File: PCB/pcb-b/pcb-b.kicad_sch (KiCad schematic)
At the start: 25 parts, among them J1 Conn_02x05_Counter_Clockwise, J2 Conn_02x05_Counter_Clockwise, K1 HK19F-DCxxV-SHC, Q13 TPCA8120,L1Q, Q3 BC817, Q9 BC817

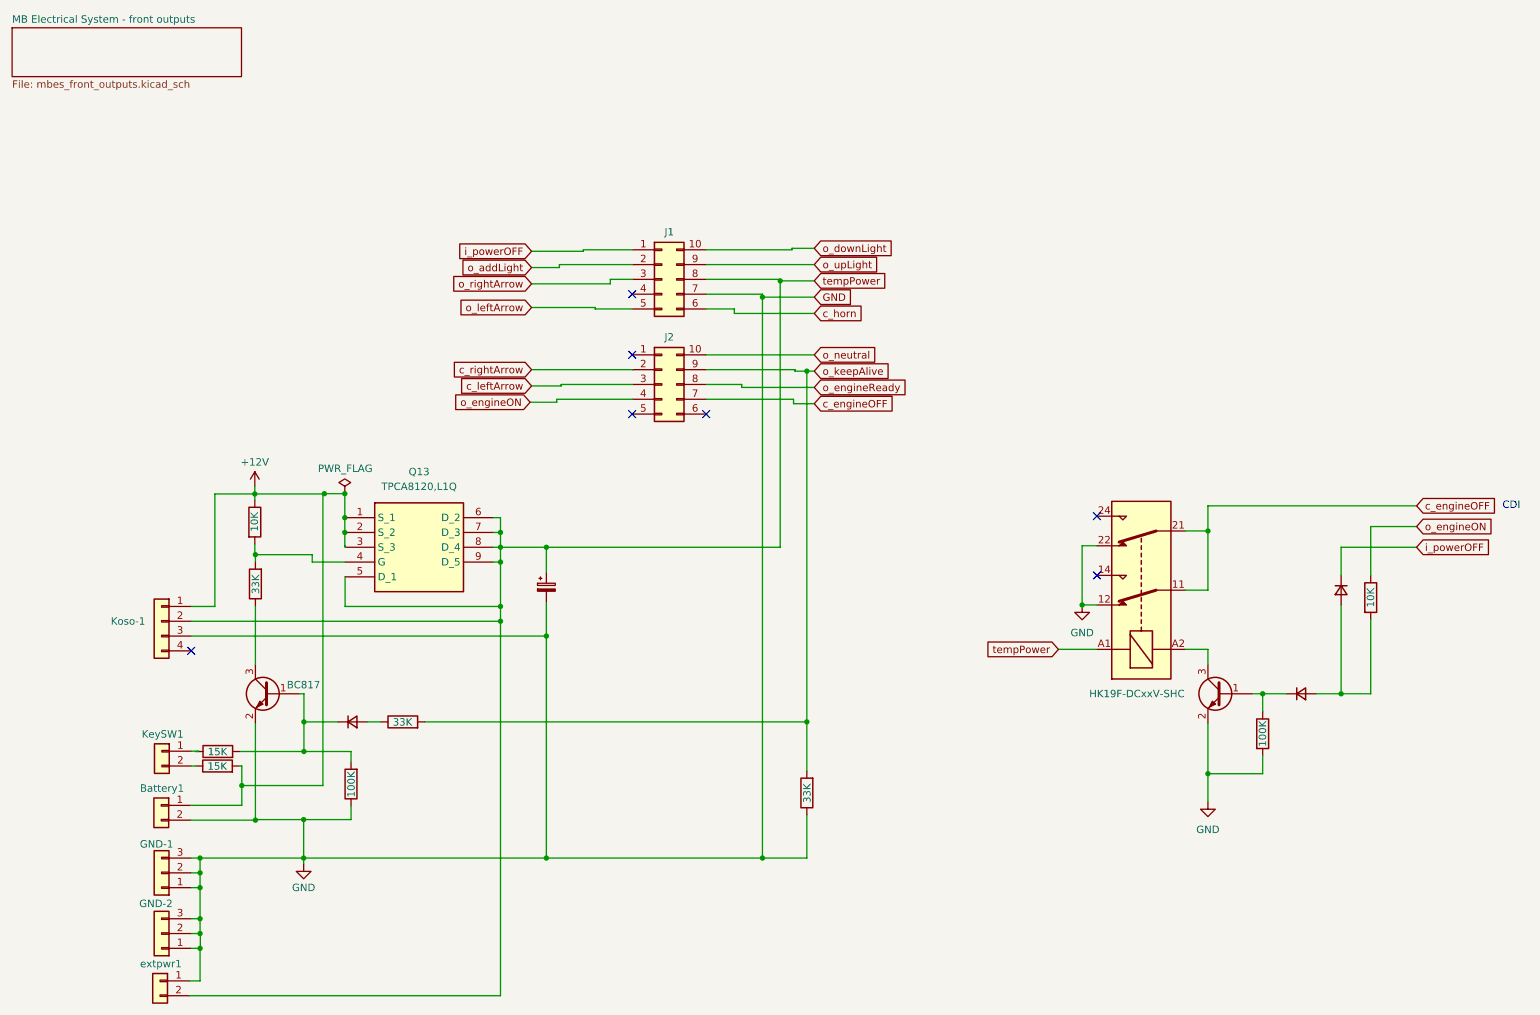
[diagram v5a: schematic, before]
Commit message: Many changes and fixes
Electric schema A & B
	- Wrong (undefined) signals direction fixed
	- More readable schema getting: c_<signal> color has changed
	- Some pull-up resistors has been added for safing purpose
	- Wire connectors holes size reducing
	- Because Led indicatord uses less then 500mA, their wire connectors have been substituted by pin-header ones

PCB
	- Updates for schema changes
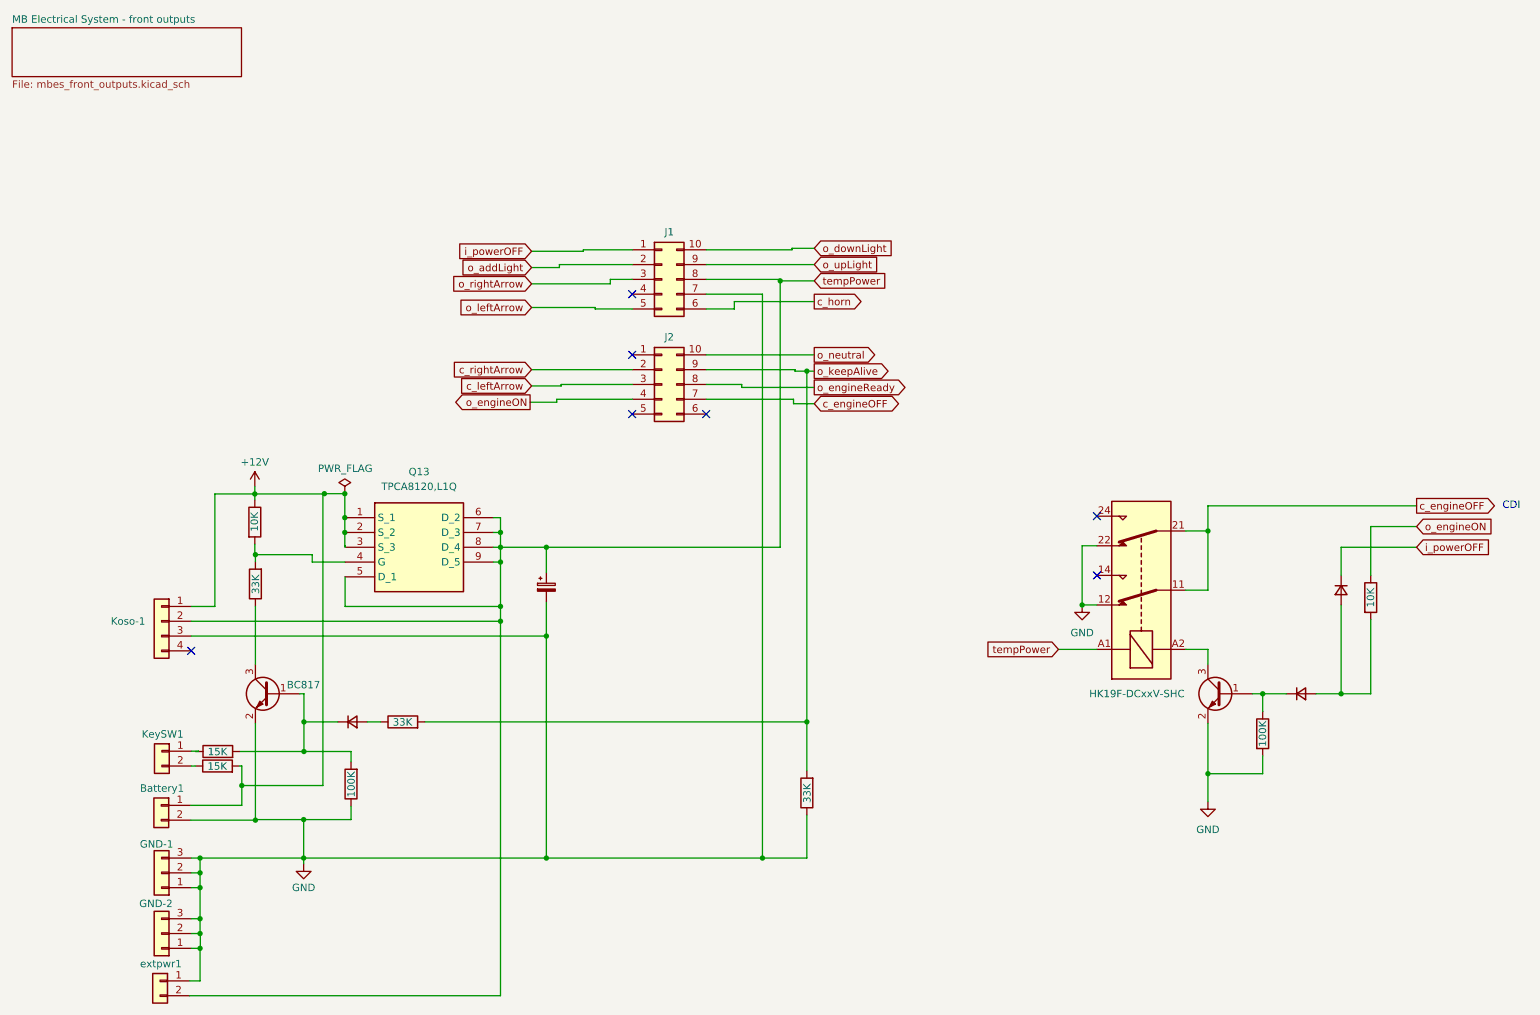
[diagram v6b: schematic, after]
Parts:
- GND-1: footprint Connector_Wire:SolderWire-1.5sqmm_1x03_P6mm_D1.7mm_OD3mm -> Connector_Wire:SolderWire-1sqmm_1x03_P5.4mm_D1.4mm_OD2.7mm
- GND-2: footprint Connector_Wire:SolderWire-1.5sqmm_1x03_P6mm_D1.7mm_OD3mm -> Connector_Wire:SolderWire-0.75sqmm_1x03_P4.8mm_D1.25mm_OD2.3mm
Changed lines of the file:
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@@
 	)
 	(junction
-		(at 142.24 62.484)
-		(diameter 0)
-		(color 0 0 0 0)
-	)
-	(junction
 		(at 45.72 174.244)
 		(diameter 0)
@@
 	(wire
 		(pts
-			(xy 137.414 65.278) (xy 151.13 65.278)
+			(xy 137.414 63.246) (xy 151.13 63.246)
 		)
 		(stroke
@@
 	(wire
 		(pts
-			(xy 142.24 62.484) (xy 142.24 158.75)
-		)
-		(stroke
-			(width 0)
-			(type default)
-		)
-	)
-	(wire
-		(pts
 			(xy 48.26 115.57) (xy 48.26 96.266)
 		)
@@
 	(wire
 		(pts
-			(xy 142.24 62.484) (xy 151.13 62.484)
-		)
-		(stroke
-			(width 0)
-			(type default)
-		)
-	)
-	(wire
-		(pts
 			(xy 45.7708 171.8564) (xy 45.72 171.8564)
 		)
@@
 	(wire
 		(pts
-			(xy 137.414 65.278) (xy 137.414 64.516)
+			(xy 137.414 63.246) (xy 137.414 64.516)
 		)
 		(stroke
@@
 	(wire
 		(pts
-			(xy 142.24 61.976) (xy 142.24 62.484)
+			(xy 142.24 61.976) (xy 142.24 158.75)
 		)
 		(stroke
@@
 		)
 	)
-	(global_label "GND"
-		(shape input)
-		(at 151.13 62.484 0)
-		(fields_autoplaced yes)
-		(effects
-			(font
-				(size 1.27 1.27)
-			)
-			(justify left)
-		)
-		(property "Intersheetrefs" "${INTERSHEET_REFS}"
-			(at 157.9857 62.484 0)
-			(effects
-				(font
-					(size 1.27 1.27)
-				)
-				(justify left)
-				(hide yes)
-			)
-		)
-		(property "Riferimenti inter-foglio" "${INTERSHEET_REFS}"
-			(at 151.13 64.6748 0)
-			(effects
-				(font
-					(size 1.27 1.27)
-				)
-				(justify left)
-				(hide yes)
-			)
-		)
-	)
 	(global_label "c_rightArrow"
 		(shape input)
@@
 			(font
 				(size 1.27 1.27)
+				(color 221 133 0 1)
 			)
 			(justify right)
 		)
 		(property "Intersheetrefs" "${INTERSHEET_REFS}"
-			(at 102.616 74.93 0)
+			(at 88.0194 74.93 0)
 			(effects
 				(font
 					(size 1.27 1.27)
 				)
+				(justify right)
 				(hide yes)
 			)
 		)
 		(property "Riferimenti inter-foglio" "${INTERSHEET_REFS}"
-			(at 88.5915 75.0094 0)
+			(at 102.616 77.1208 0)
 			(effects
 				(font
@@
 	)
 	(global_label "c_horn"
-		(shape input)
-		(at 151.13 65.278 0)
+		(shape output)
+		(at 151.13 63.246 0)
 		(fields_autoplaced yes)
 		(effects
 			(font
 				(size 1.27 1.27)
+				(color 221 133 0 1)
 			)
 			(justify left)
 		)
 		(property "Intersheetrefs" "${INTERSHEET_REFS}"
-			(at 160.4046 65.278 0)
+			(at 160.4046 63.246 0)
 			(effects
 				(font
@@
 		)
 		(property "Riferimenti inter-foglio" "${INTERSHEET_REFS}"
-			(at 151.13 67.4688 0)
+			(at 151.13 65.4368 0)
 			(effects
 				(font
@@
 	)
 	(global_label "o_keepAlive"
-		(shape input)
+		(shape output)
 		(at 151.13 75.184 0)
 		(fields_autoplaced yes)
@@
 		)
 		(property "Intersheetrefs" "${INTERSHEET_REFS}"
-			(at 151.13 75.184 0)
+			(at 165.0009 75.184 0)
 			(effects
 				(font
 					(size 1.27 1.27)
 				)
+				(justify left)
 				(hide yes)
 			)
 		)
 		(property "Riferimenti inter-foglio" "${INTERSHEET_REFS}"
-			(at 164.4288 75.1046 0)
+			(at 151.13 77.3748 0)
 			(effects
 				(font
@@
 			(font
 				(size 1.27 1.27)
+				(color 221 133 0 1)
 			)
 			(justify right)
@@
 	)
 	(global_label "o_engineReady"
-		(shape input)
+		(shape output)
 		(at 151.13 77.978 0)
 		(fields_autoplaced yes)
@@
 		)
 		(property "Intersheetrefs" "${INTERSHEET_REFS}"
-			(at 151.13 77.978 0)
+			(at 168.085 77.978 0)
 			(effects
 				(font
 					(size 1.27 1.27)
 				)
+				(justify left)
 				(hide yes)
 			)
 		)
 		(property "Riferimenti inter-foglio" "${INTERSHEET_REFS}"
-			(at 167.5131 77.8986 0)
+			(at 151.13 80.1688 0)
 			(effects
 				(font
@@
 	)
 	(global_label "c_engineOFF"
-		(shape input)
+		(shape bidirectional)
 		(at 151.13 80.772 0)
 		(fields_autoplaced yes)
@@
 			(font
 				(size 1.27 1.27)
+				(color 221 133 0 1)
 			)
 			(justify left)
 		)
 		(property "Intersheetrefs" "${INTERSHEET_REFS}"
-			(at 165.9081 80.772 0)
+			(at 167.0194 80.772 0)
 			(effects
 				(font
@@
 	)
 	(global_label "o_neutral"
-		(shape input)
+		(shape output)
 		(at 151.13 72.39 0)
 		(fields_autoplaced yes)
@@
 	)
 	(global_label "c_engineOFF"
-		(shape input)
+		(shape output)
 		(at 254.508 98.298 0)
 		(fields_autoplaced yes)
@@
 			(font
 				(size 1.27 1.27)
+				(color 221 133 0 1)
 			)
 			(justify left)
 		)
 		(property "Intersheetrefs" "${INTERSHEET_REFS}"
-			(at 254.508 98.298 0)
+			(at 269.2861 98.298 0)
 			(effects
 				(font
 					(size 1.27 1.27)
 				)
+				(justify left)
 				(hide yes)
 			)
 		)
 		(property "Riferimenti inter-foglio" "${INTERSHEET_REFS}"
-			(at 268.714 98.2186 0)
+			(at 254.508 100.4888 0)
 			(effects
 				(font
@@
 	)
 	(global_label "o_engineON"
-		(shape input)
+		(shape output)
 		(at 102.362 80.518 180)
 		(fields_autoplaced yes)
@@
 		)
 		(property "Intersheetrefs" "${INTERSHEET_REFS}"
-			(at 102.362 80.518 0)
+			(at 88.3702 80.518 0)
 			(effects
 				(font
 					(size 1.27 1.27)
 				)
+				(justify right)
 				(hide yes)
 			)
 		)
 		(property "Riferimenti inter-foglio" "${INTERSHEET_REFS}"
-			(at 88.9422 80.4386 0)
+			(at 102.362 82.7088 0)
 			(effects
 				(font
@@
 			)
 		)
-		(property "Footprint" "Connector_Wire:SolderWire-1.5sqmm_1x03_P6mm_D1.7mm_OD3mm"
+		(property "Footprint" "Connector_Wire:SolderWire-1sqmm_1x03_P5.4mm_D1.4mm_OD2.7mm"
 			(at 39.116 161.29 0)
 			(effects
@@
 			)
 		)
-		(property "Footprint" "Connector_Wire:SolderWire-1.5sqmm_1x03_P6mm_D1.7mm_OD3mm"
+		(property "Footprint" "Connector_Wire:SolderWire-0.75sqmm_1x03_P4.8mm_D1.25mm_OD2.3mm"
 			(at 39.116 171.704 0)
 			(effects

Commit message: Small changes for the Title block
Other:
- company: Panicosoft -> https://github.com/catinella/mbElectricalSystem
- title: Motorbike lights and services controller -> Power stage
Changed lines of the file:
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@@
 	(paper "A4")
 	(title_block
-		(title "Motorbike lights and services controller")
-		(date "2022-08-24")
-		(rev "4.0")
-		(company "Panicosoft")
+		(title "Power stage")
+		(company "https://github.com/catinella/mbElectricalSystem")
 	)
 	(bus_alias "port-b"

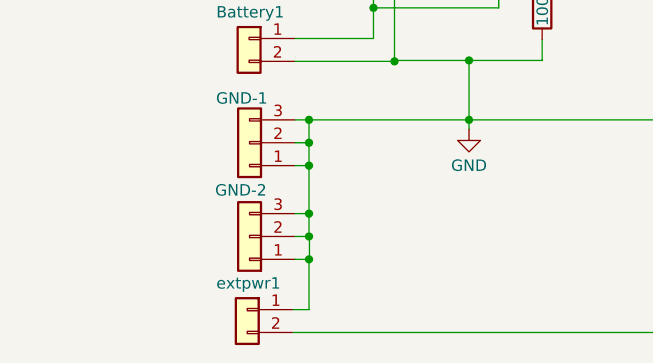
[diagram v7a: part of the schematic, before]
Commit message: External power connector is now used for rear power stage
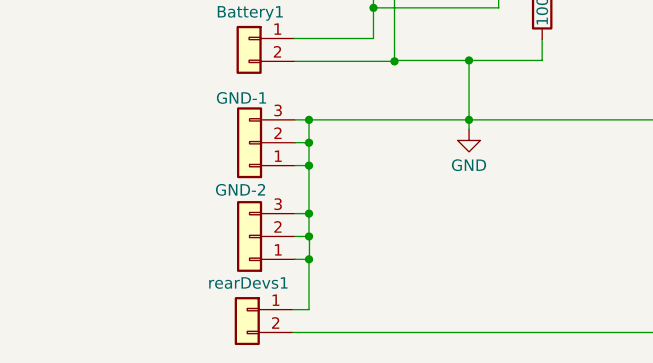
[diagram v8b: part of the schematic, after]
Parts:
- renumbered extpwr1 to rearDevs1
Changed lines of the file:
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@@
 		(on_board yes)
 		(dnp no)
-		(property "Reference" "extpwr1"
+		(property "Reference" "rearDevs1"
 			(at 38.989 176.911 0)
 			(effects
@@
 			(project "pcb-b"
 				(path "/709d0967-afe5-49d3-92a5-d2bb94550bdb"
-					(reference "extpwr1")
+					(reference "rearDevs1")
 					(unit 1)
 				)
